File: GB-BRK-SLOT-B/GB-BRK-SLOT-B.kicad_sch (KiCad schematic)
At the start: 24 parts

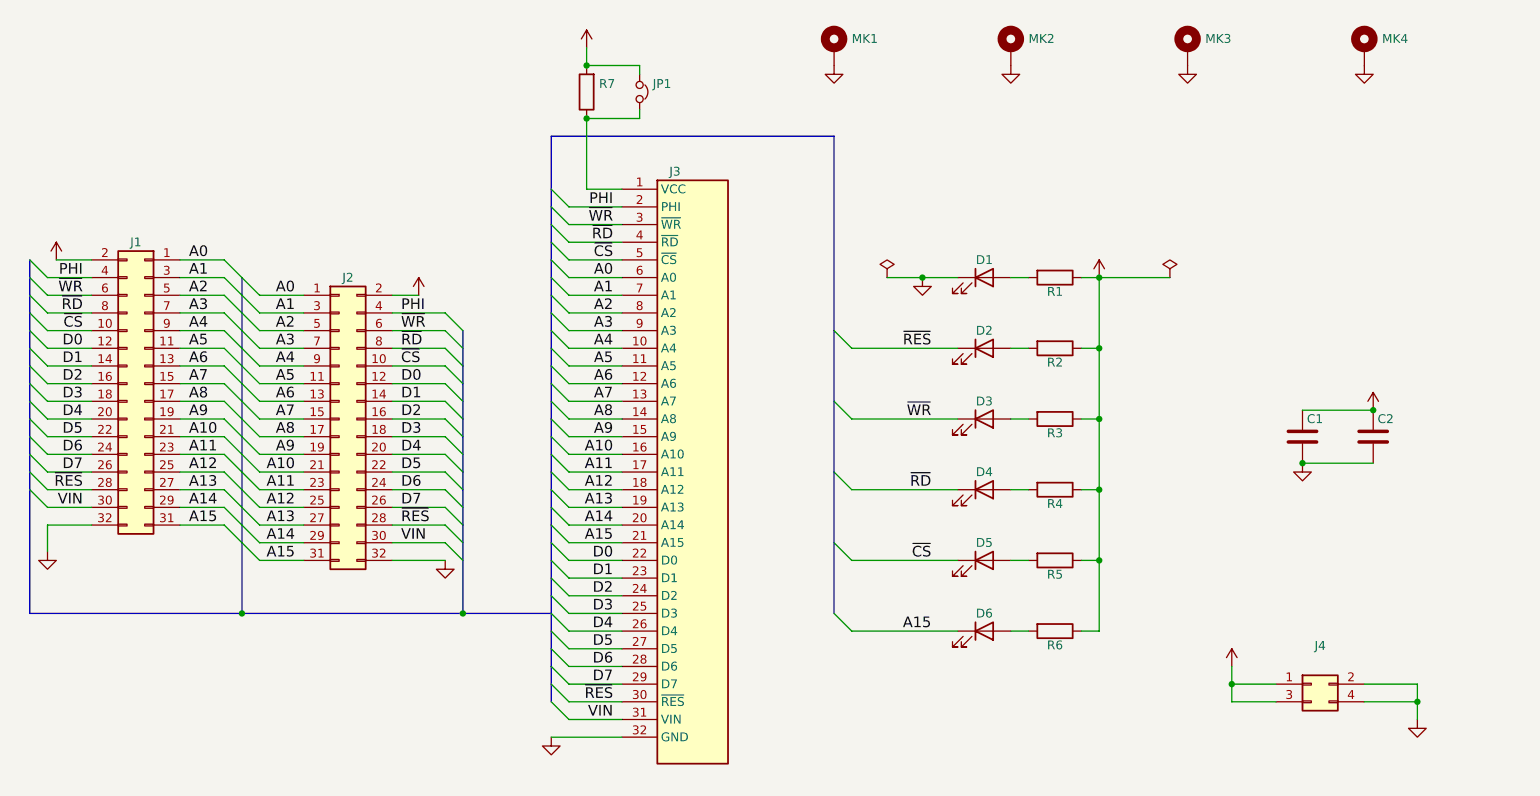
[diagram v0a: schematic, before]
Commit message: Upgrade projects to KiCad 7
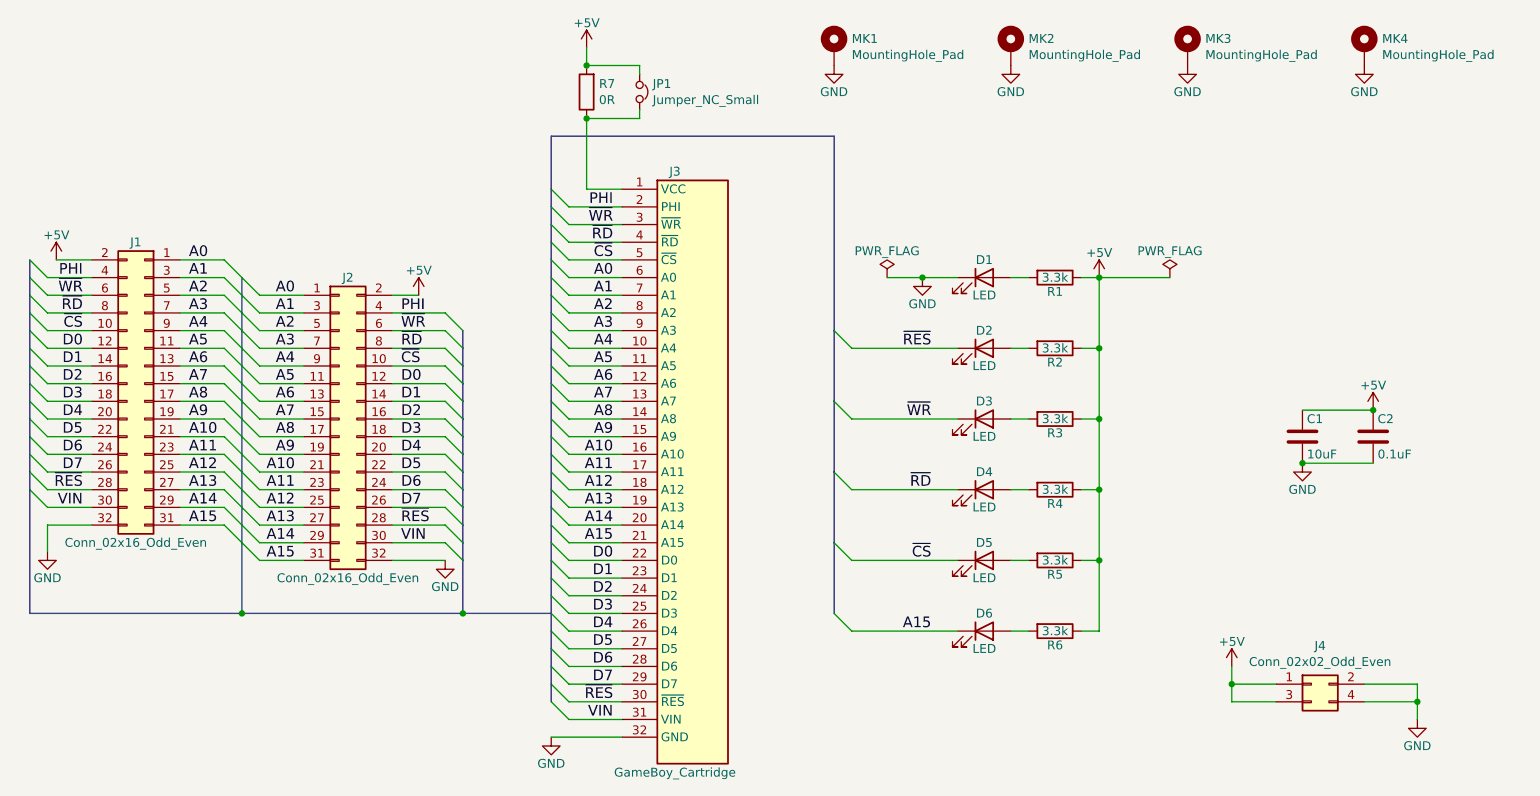
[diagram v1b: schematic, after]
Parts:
- C1: value (none) -> 10uF; footprint (none) -> Capacitor_SMD:C_1206_3216Metric
- C2: value (none) -> 0.1uF; footprint (none) -> Capacitor_SMD:C_0603_1608Metric
- D1, D2, D3, D4, D5, D6: value (none) -> LED; footprint (none) -> LED_SMD:LED_0603_1608Metric
- J1: value (none) -> Conn_02x16_Odd_Even; footprint (none) -> Connector_PinSocket_2.54mm:PinSocket_2x16_P2.54mm_Vertical
- J2: value (none) -> Conn_02x16_Odd_Even; footprint (none) -> Connector_PinHeader_2.54mm:PinHeader_2x16_P2.54mm_Vertical
- J3: value (none) -> GameBoy_Cartridge; footprint (none) -> Gekkio_Connector_PCBedge:GameBoy_Cartridge_SGB-SGB2_1x32_P1.50mm_Socket_Horizontal
- J4: value (none) -> Conn_02x02_Odd_Even; footprint (none) -> Connector_PinHeader_2.54mm:PinHeader_2x02_P2.54mm_Vertical
- JP1: value (none) -> Jumper_NC_Small; footprint (none) -> Connector_PinHeader_2.54mm:PinHeader_1x02_P2.54mm_Vertical
- MK1, MK2, MK3, MK4: value (none) -> MountingHole_Pad; footprint (none) -> MountingHole:MountingHole_3.2mm_M3_Pad_Via
- R1, R2, R3, R4, R5, R6: value (none) -> 3.3k; footprint (none) -> Resistor_SMD:R_0603_1608Metric
- R7: value (none) -> 0R; footprint (none) -> Resistor_SMD:R_1206_3216Metric_Pad1.42x1.75mm_HandSolder
